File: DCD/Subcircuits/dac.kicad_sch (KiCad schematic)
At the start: 23 parts, among them U10 DAC8811ICDGKT, U11 OPA277UA, U12 OPA277UA, U8 OPA277UA, U9 DAC8811ICDGKT

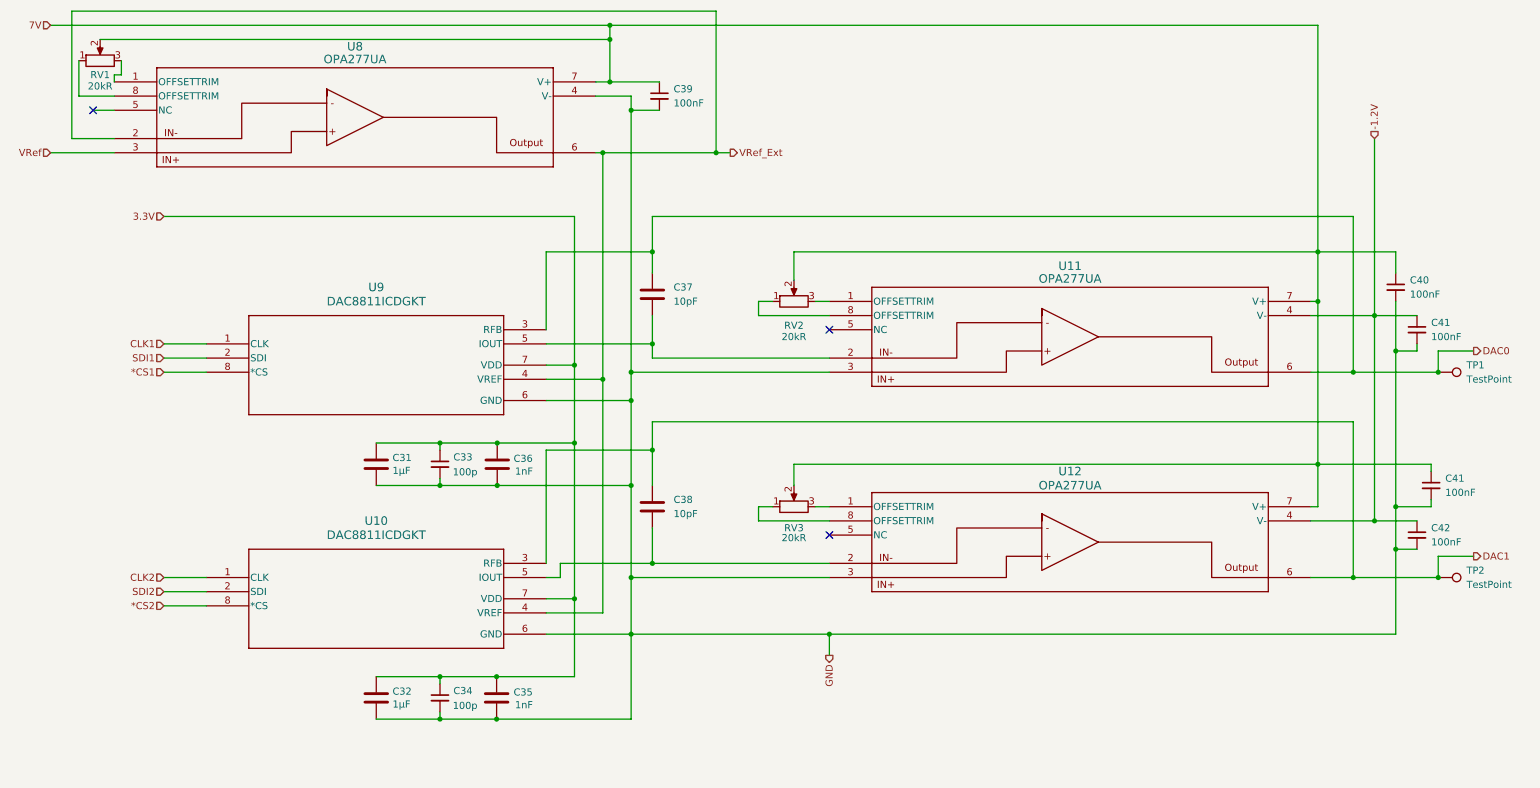
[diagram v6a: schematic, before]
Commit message: Finished
Final touches, PSUs filtering, external connections, psu connections for
the negative voltage, and the DAC higher voltage, and the negative
voltage. Added an external connection directely to the DAC.
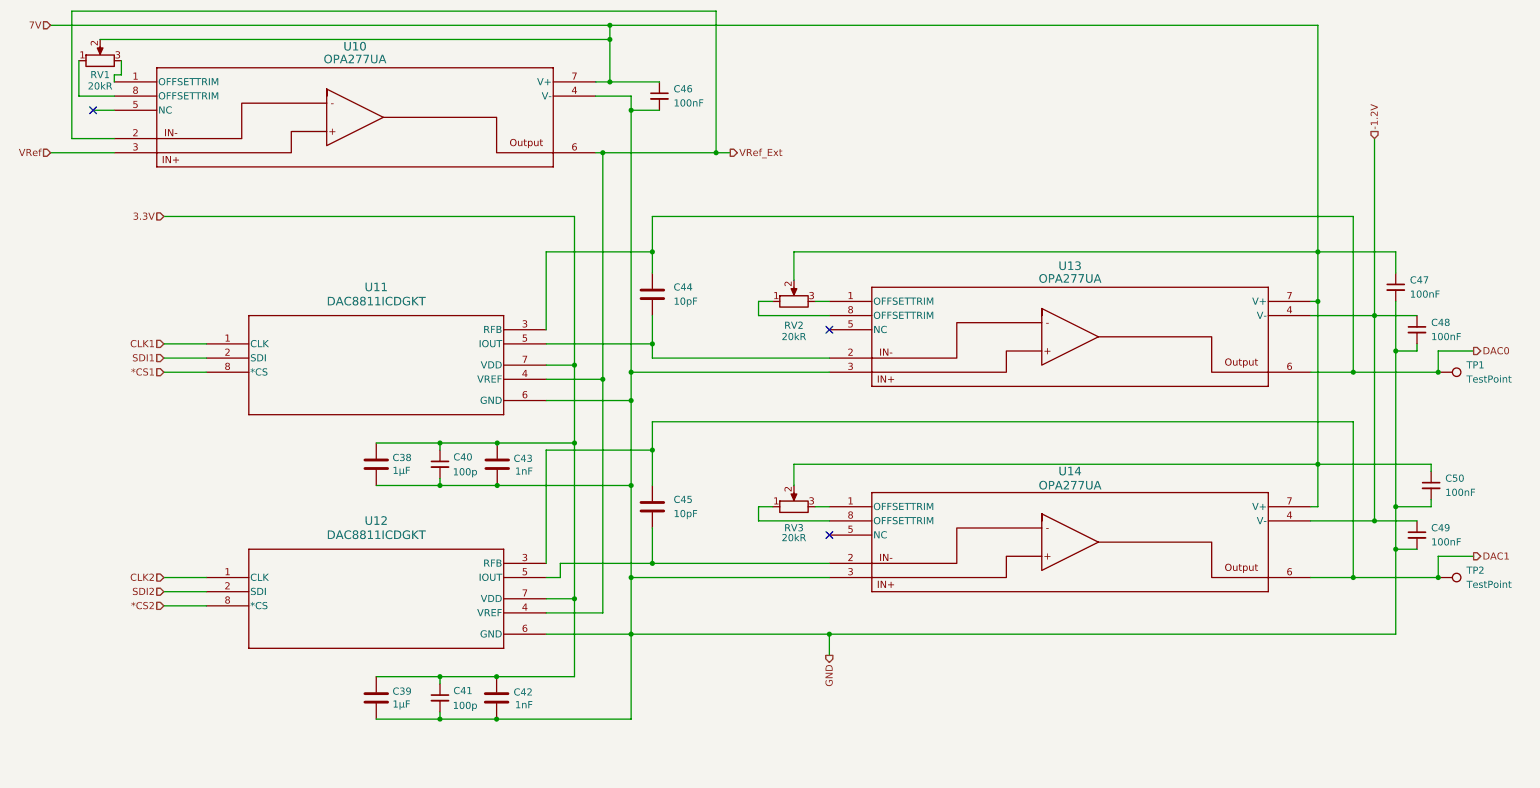
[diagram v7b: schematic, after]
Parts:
- renumbered C31 to C38, C32 to C39, C33 to C40, C34 to C41, C35 to C42, C36 to C43, C37 to C44, C38 to C45, C39 to C46, C40 to C47, C41 to C48, C42 to C49, C41 to C50, U8 to U10, U9 to U11, U10 to U12, U11 to U13, U12 to U14
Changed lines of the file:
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@@
 		(on_board yes)
 		(dnp no)
-		(property "Reference" "C34"
+		(property "Reference" "C41"
 			(at 97.282 148.59 0)
 			(effects
@@
 			(project "DCD"
 				(path "/b8e3d55b-fa56-4199-88ad-60cfd98f56f9/6102592d-9e5a-4d16-a1d9-3adb4d835efe"
-					(reference "C34")
+					(reference "C41")
 					(unit 1)
 				)
@@
 		(on_board yes)
 		(dnp no)
-		(property "Reference" "C41"
+		(property "Reference" "C50"
 			(at 271.78 110.49 0)
 			(effects
@@
 			(project "DCD"
 				(path "/b8e3d55b-fa56-4199-88ad-60cfd98f56f9/6102592d-9e5a-4d16-a1d9-3adb4d835efe"
-					(reference "C41")
+					(reference "C50")
 					(unit 1)
 				)
@@
 		(on_board yes)
 		(dnp no)
-		(property "Reference" "C41"
+		(property "Reference" "C48"
 			(at 269.24 82.55 0)
 			(effects
@@
 			(project "DCD"
 				(path "/b8e3d55b-fa56-4199-88ad-60cfd98f56f9/6102592d-9e5a-4d16-a1d9-3adb4d835efe"
-					(reference "C41")
+					(reference "C48")
 					(unit 1)
 				)
@@
 		(on_board yes)
 		(dnp no)
-		(property "Reference" "C35"
+		(property "Reference" "C42"
 			(at 104.648 148.844 0)
 			(effects
@@
 			(project "DCD"
 				(path "/b8e3d55b-fa56-4199-88ad-60cfd98f56f9/6102592d-9e5a-4d16-a1d9-3adb4d835efe"
-					(reference "C35")
+					(reference "C42")
 					(unit 1)
 				)
@@
 		(on_board yes)
 		(dnp no)
-		(property "Reference" "C40"
+		(property "Reference" "C47"
 			(at 265.43 74.93 0)
 			(effects
@@
 			(project "DCD"
 				(path "/b8e3d55b-fa56-4199-88ad-60cfd98f56f9/6102592d-9e5a-4d16-a1d9-3adb4d835efe"
-					(reference "C40")
+					(reference "C47")
 					(unit 1)
 				)
@@
 		(dnp no)
 		(fields_autoplaced yes)
-		(property "Reference" "C37"
+		(property "Reference" "C44"
 			(at 133.35 76.1999 0)
 			(effects
@@
 			(project "DCD"
 				(path "/b8e3d55b-fa56-4199-88ad-60cfd98f56f9/6102592d-9e5a-4d16-a1d9-3adb4d835efe"
-					(reference "C37")
+					(reference "C44")
 					(unit 1)
 				)
@@
 		(dnp no)
 		(fields_autoplaced yes)
-		(property "Reference" "U10"
+		(property "Reference" "U12"
 			(at 80.01 118.11 0)
 			(effects
@@
 			(project "DCD"
 				(path "/b8e3d55b-fa56-4199-88ad-60cfd98f56f9/6102592d-9e5a-4d16-a1d9-3adb4d835efe"
-					(reference "U10")
+					(reference "U12")
 					(unit 1)
 				)
@@
 		(on_board yes)
 		(dnp no)
-		(property "Reference" "C36"
+		(property "Reference" "C43"
 			(at 104.648 106.934 0)
 			(effects
@@
 			(project "DCD"
 				(path "/b8e3d55b-fa56-4199-88ad-60cfd98f56f9/6102592d-9e5a-4d16-a1d9-3adb4d835efe"
-					(reference "C36")
+					(reference "C43")
 					(unit 1)
 				)
@@
 		(on_board yes)
 		(dnp no)
-		(property "Reference" "C31"
+		(property "Reference" "C38"
 			(at 82.931 106.7816 0)
 			(effects
@@
 			(project "DCD"
 				(path "/b8e3d55b-fa56-4199-88ad-60cfd98f56f9/6102592d-9e5a-4d16-a1d9-3adb4d835efe"
-					(reference "C31")
+					(reference "C38")
 					(unit 1)
 				)
@@
 		(on_board yes)
 		(dnp no)
-		(property "Reference" "C39"
+		(property "Reference" "C46"
 			(at 133.35 40.64 0)
 			(effects
@@
 			(project "DCD"
 				(path "/b8e3d55b-fa56-4199-88ad-60cfd98f56f9/6102592d-9e5a-4d16-a1d9-3adb4d835efe"
-					(reference "C39")
+					(reference "C46")
 					(unit 1)
 				)
@@
 		(dnp no)
 		(fields_autoplaced yes)
-		(property "Reference" "U9"
+		(property "Reference" "U11"
 			(at 80.01 76.2 0)
 			(effects
@@
 			(project "DCD"
 				(path "/b8e3d55b-fa56-4199-88ad-60cfd98f56f9/6102592d-9e5a-4d16-a1d9-3adb4d835efe"
-					(reference "U9")
+					(reference "U11")
 					(unit 1)
 				)
@@
 		(on_board yes)
 		(dnp no)
-		(property "Reference" "U12"
+		(property "Reference" "U14"
 			(at 204.47 109.22 0)
 			(effects
@@
 			(project "DCD"
 				(path "/b8e3d55b-fa56-4199-88ad-60cfd98f56f9/6102592d-9e5a-4d16-a1d9-3adb4d835efe"
-					(reference "U12")
+					(reference "U14")
 					(unit 1)
 				)
@@
 		(on_board yes)
 		(dnp no)
-		(property "Reference" "C32"
+		(property "Reference" "C39"
 			(at 82.931 148.6916 0)
 			(effects
@@
 			(project "DCD"
 				(path "/b8e3d55b-fa56-4199-88ad-60cfd98f56f9/6102592d-9e5a-4d16-a1d9-3adb4d835efe"
-					(reference "C32")
+					(reference "C39")
 					(unit 1)
 				)
@@
 		(on_board yes)
 		(dnp no)
-		(property "Reference" "U8"
+		(property "Reference" "U10"
 			(at 76.2 33.02 0)
 			(effects
@@
 			(project "DCD"
 				(path "/b8e3d55b-fa56-4199-88ad-60cfd98f56f9/6102592d-9e5a-4d16-a1d9-3adb4d835efe"
-					(reference "U8")
+					(reference "U10")
 					(unit 1)
 				)
@@
 		(on_board yes)
 		(dnp no)
-		(property "Reference" "C42"
+		(property "Reference" "C49"
 			(at 269.24 119.38 0)
 			(effects
@@
 			(project "DCD"
 				(path "/b8e3d55b-fa56-4199-88ad-60cfd98f56f9/6102592d-9e5a-4d16-a1d9-3adb4d835efe"
-					(reference "C42")
+					(reference "C49")
 					(unit 1)
 				)
@@
 		(on_board yes)
 		(dnp no)
-		(property "Reference" "C33"
+		(property "Reference" "C40"
 			(at 97.282 106.68 0)
 			(effects
@@
 			(project "DCD"
 				(path "/b8e3d55b-fa56-4199-88ad-60cfd98f56f9/6102592d-9e5a-4d16-a1d9-3adb4d835efe"
-					(reference "C33")
+					(reference "C40")
 					(unit 1)
 				)
@@
 		(on_board yes)
 		(dnp no)
-		(property "Reference" "U11"
+		(property "Reference" "U13"
 			(at 204.47 72.39 0)
 			(effects
@@
 			(project ""
 				(path "/b8e3d55b-fa56-4199-88ad-60cfd98f56f9/6102592d-9e5a-4d16-a1d9-3adb4d835efe"
-					(reference "U11")
+					(reference "U13")
 					(unit 1)
 				)
@@
 		(dnp no)
 		(fields_autoplaced yes)
-		(property "Reference" "C38"
+		(property "Reference" "C45"
 			(at 133.35 114.2999 0)
 			(effects
@@
 			(project "DCD"
 				(path "/b8e3d55b-fa56-4199-88ad-60cfd98f56f9/6102592d-9e5a-4d16-a1d9-3adb4d835efe"
-					(reference "C38")
+					(reference "C45")
 					(unit 1)
 				)

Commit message: Progress on the layout
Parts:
- added FB18, FB19: 470Ω, Inductor_SMD:L_0603_1608Metric, symbol Device:FerriteBead_Small
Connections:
- net GND renamed AGND
- net AGND: now also FB18.2, FB19.2; no longer C38.2, C39.2, C40.2, C41.2, C42.2, C43.2
- new net DGND: C38.2, C39.2, C40.2, C41.2, C42.2, C43.2, FB18.1, FB19.1
